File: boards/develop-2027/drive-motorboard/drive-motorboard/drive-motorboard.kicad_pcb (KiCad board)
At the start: 2 copper layers, 0 parts

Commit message: WIP layout draft
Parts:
- added C1: 100u 35V, Capacitor_SMD:C_Elec_6.3x5.8, B.Cu at (59.0, 66.0)
- added C10: 100n 10V, Capacitor_SMD:C_0402_1005Metric, F.Cu at (88.5, 85.2)
- added C11: 1n, Capacitor_SMD:C_0402_1005Metric, B.Cu at (77.2, 91.2)
- added C12: 1u 63V, Capacitor_SMD:C_0603_1608Metric, B.Cu at (73.5, 78.5)
- added C13: 1u 63V, Capacitor_SMD:C_0603_1608Metric, B.Cu at (70.5, 78.5)
- added C14: 1u 63V, Capacitor_SMD:C_0603_1608Metric, B.Cu at (67.5, 78.5)
- added C15: 1u 63V, Capacitor_SMD:C_0603_1608Metric, B.Cu at (64.5, 78.5)
- added C16: 1u 63V, Capacitor_SMD:C_0603_1608Metric, B.Cu at (61.5, 78.5)
- added C17: 1u 63V, Capacitor_SMD:C_0603_1608Metric, B.Cu at (58.5, 78.5)
- added C18: 100n 10V, Capacitor_SMD:C_0402_1005Metric, B.Cu at (83.2, 91.1)
- added C19: 100n 10V, Capacitor_SMD:C_0402_1005Metric, F.Cu at (70.6, 75.0)
- added C2: 1u 10V, Capacitor_SMD:C_0603_1608Metric, B.Cu at (91.0, 83.2)
- added C20: 1u 63V, Capacitor_SMD:C_0603_1608Metric, F.Cu at (145.8, 52.8)
- added C21: 10u 25V, Capacitor_SMD:C_0603_1608Metric, F.Cu at (145.8, 55.3)
- added C22: 10u 25V, Capacitor_SMD:C_0603_1608Metric, F.Cu at (145.8, 57.8)
- added C23: 100n 10V, Capacitor_SMD:C_0402_1005Metric, B.Cu at (53.5, 91.2)
- added C3: 1u 63V, Capacitor_SMD:C_0603_1608Metric, F.Cu at (79.6, 82.2)
- added C4: 1u 63V, Capacitor_SMD:C_0603_1608Metric, F.Cu at (79.6, 84.2)
- added C5: 1u 63V, Capacitor_SMD:C_0603_1608Metric, F.Cu at (79.6, 86.2)
- added C6: 100u 35V, Capacitor_SMD:C_Elec_6.3x5.8, B.Cu at (59.0, 73.8)
- added C7: 100n 10V, Capacitor_SMD:C_0402_1005Metric, B.Cu at (89.8, 83.8)
- added C8: 1u 63V, Capacitor_SMD:C_0603_1608Metric, B.Cu at (90.0, 86.2)
- added C9: 10u 25V, Capacitor_SMD:C_0603_1608Metric, F.Cu at (89.8, 85.5)
- added D1: FAULT, LED_SMD:LED_0603_1608Metric, F.Cu at (113.3, 74.7)
- added D10: PUSB3FR4Z, Package_DFN_QFN:Diodes_UDFN-10_1x2.5mm_P0.5mm, F.Cu at (124.5, 89.7)
- added D11: SMAJ22A, Diode_SMD:D_SMA, F.Cu at (147.8, 61.3)
- added D12: VBATT PWR, LED_SMD:LED_0603_1608Metric, F.Cu at (149.8, 57.4)
- added D2: 1N4148WL2-TP, Diode_SMD:D_SOD-882, B.Cu at (78.4, 81.5)
- added D3: 1N4148WL2-TP, Diode_SMD:D_SOD-882, B.Cu at (78.4, 79.5)
- added D4: 1N4148WL2-TP, Diode_SMD:D_SOD-882, B.Cu at (78.4, 85.5)
- added D5: 1N4148WL2-TP, Diode_SMD:D_SOD-882, B.Cu at (78.4, 83.5)
- added D6: 1N4148WL2-TP, Diode_SMD:D_SOD-882, B.Cu at (78.4, 89.5)
- added D7: 1N4148WL2-TP, Diode_SMD:D_SOD-882, B.Cu at (78.4, 87.5)
- added D8: PUSB3FR4Z, Package_DFN_QFN:Diodes_UDFN-10_1x2.5mm_P0.5mm, F.Cu at (83.0, 93.0)
- added D9: PUSB3FR4Z, Package_DFN_QFN:Diodes_UDFN-10_1x2.5mm_P0.5mm, F.Cu at (21.2, 69.2)
- added F1: 10A 60V, RJ-Passives:Fuse_2410_6125Metric, F.Cu at (148.1, 65.9)
- added H1: Motor Mount, MountingHole:MountingHole_3.2mm_M3_Pad, F.Cu at (96.0, 54.0)
- added H2: Motor Mount, MountingHole:MountingHole_3.2mm_M3_Pad, F.Cu at (96.0, 96.0)
- added H3: Motor Mount, MountingHole:MountingHole_3.2mm_M3_Pad, F.Cu at (54.0, 96.0)
- added H4: Motor Mount, MountingHole:MountingHole_3.2mm_M3_Pad, F.Cu at (54.0, 54.0)
- added J1: MOTOR HALL, Connector_JST:JST_ACH_BM05B-ACHSS-A-GAN-ETF_1x05-1MP_P1.20mm_Vertical, F.Cu at (83.0, 97.0)
- added J2: MOTOR UVW, Connector_JST:JST_ACH_BM03B-ACHSS-GAN-ETF_1x03-1MP_P1.20mm_Vertical, F.Cu at (66.0, 97.0)
- added J3: PROG SPI, Connector_JST:JST_GH_SM06B-GHS-TB_1x06-1MP_P1.25mm_Horizontal, F.Cu at (21.2, 64.2)
- added J4: COMM SPI, Connector_JST:JST_GH_SM06B-GHS-TB_1x06-1MP_P1.25mm_Horizontal, F.Cu at (85.0, 55.0)
- added J5: Conn_ST_STDC14, Connector:Tag-Connect_TC2070-IDC-FP_2x07_P1.27mm_Vertical, B.Cu at (92.0, 70.5)
- added J6: PWR_IN, Connector_JST:JST_VH_B2PS-VH_1x02_P3.96mm_Horizontal, F.Cu at (136.8, 53.9)
- added L1: 10u 540mA, Inductor_SMD:L_1210_3225Metric, F.Cu at (146.6, 70.2)
- added Q1: STL90N10F7, Package_DFN_QFN:PQFN-8-EP_6x5mm_P1.27mm_Generic, B.Cu at (72.0, 83.0)
- added Q2: STL90N10F7, Package_DFN_QFN:PQFN-8-EP_6x5mm_P1.27mm_Generic, B.Cu at (72.0, 90.5)
- added Q3: STL90N10F7, Package_DFN_QFN:PQFN-8-EP_6x5mm_P1.27mm_Generic, B.Cu at (66.0, 83.0)
- added Q4: STL90N10F7, Package_DFN_QFN:PQFN-8-EP_6x5mm_P1.27mm_Generic, B.Cu at (66.0, 90.5)
- added Q5: STL90N10F7, Package_DFN_QFN:PQFN-8-EP_6x5mm_P1.27mm_Generic, B.Cu at (60.0, 83.0)
- added Q6: STL90N10F7, Package_DFN_QFN:PQFN-8-EP_6x5mm_P1.27mm_Generic, B.Cu at (60.0, 90.5)
- added R1: 15m ±1% 3W, RJ-Passives:R_Shunt_Analog_2512_6332_HighAccuracy, B.Cu at (78.0, 97.0)
- added R10: 0R, Resistor_SMD:R_0402_1005Metric, B.Cu at (76.8, 79.0)
- added R11: 68R, Resistor_SMD:R_0402_1005Metric, B.Cu at (76.8, 85.0)
- added R12: 68R, Resistor_SMD:R_0402_1005Metric, B.Cu at (76.8, 84.0)
- added R13: 0R, Resistor_SMD:R_0402_1005Metric, B.Cu at (76.8, 86.0)
- added R14: 0R, Resistor_SMD:R_0402_1005Metric, B.Cu at (76.8, 83.0)
- added R15: 68R, Resistor_SMD:R_0402_1005Metric, B.Cu at (76.8, 89.0)
- added R16: 68R, Resistor_SMD:R_0402_1005Metric, B.Cu at (76.8, 88.0)
- added R17: 0R, Resistor_SMD:R_0402_1005Metric, B.Cu at (76.8, 90.0)
- added R18: 0R, Resistor_SMD:R_0402_1005Metric, B.Cu at (76.8, 87.0)
- added R19: 1.13k ±0.1%, Resistor_SMD:R_0402_1005Metric, B.Cu at (77.8, 93.8)
- added R2: 10k, Resistor_SMD:R_0402_1005Metric, F.Cu at (126.6, 52.5)
- added R20: 16.5k ±0.1%, Resistor_SMD:R_0402_1005Metric, F.Cu at (77.2, 92.2)
- added R21: 16.5k ±0.1%, Resistor_SMD:R_0402_1005Metric, F.Cu at (77.2, 91.2)
- added R22: 1.13k ±0.1%, Resistor_SMD:R_0402_1005Metric, B.Cu at (79.2, 93.8)
- added R23: 8.25k ±0.5%, Resistor_SMD:R_0201_0603Metric, B.Cu at (83.0, 89.5)
- added R24: 300R ±1%, Resistor_SMD:R_0201_0603Metric, B.Cu at (83.5, 90.2)
- added R25: 10k, Resistor_SMD:R_0402_1005Metric, B.Cu at (88.5, 79.8)
- added R26: 10k, Resistor_SMD:R_0402_1005Metric, B.Cu at (87.5, 79.8)
- added R27: 10k, Resistor_SMD:R_0402_1005Metric, B.Cu at (85.2, 79.8)
- added R28: 10k, Resistor_SMD:R_0402_1005Metric, B.Cu at (21.8, 64.0)
- added R29: 10k, Resistor_SMD:R_0402_1005Metric, B.Cu at (19.4, 64.0)
- added R3: 10k, Resistor_SMD:R_0402_1005Metric, F.Cu at (89.2, 83.2)
- added R30: 10k, Resistor_SMD:R_0402_1005Metric, B.Cu at (23.0, 64.0)
- added R31: 4.7k, Resistor_SMD:R_0402_1005Metric, F.Cu at (53.8, 87.2)
- added R32: 4.7k, Resistor_SMD:R_0402_1005Metric, F.Cu at (54.8, 87.2)
- added R33: 10k, Resistor_SMD:R_0402_1005Metric, F.Cu at (126.7, 79.0)
- added R34: 100, Resistor_SMD:R_0402_1005Metric, F.Cu at (92.0, 68.4)
- added R35: 100k, Resistor_SMD:R_0402_1005Metric, F.Cu at (150.8, 69.1)
- added R36: 10k, Resistor_SMD:R_0402_1005Metric, F.Cu at (150.8, 71.1)
- added R4: 1.13k ±0.1%, Resistor_SMD:R_0402_1005Metric, B.Cu at (76.8, 93.8)
- added R5: 33k ±0.1%, Resistor_SMD:R_0402_1005Metric, B.Cu at (77.2, 92.2)
- added R6: 10k, Resistor_SMD:R_0402_1005Metric, F.Cu at (126.6, 60.5)
- added R7: 68R, Resistor_SMD:R_0402_1005Metric, B.Cu at (76.8, 81.0)
- added R8: 68R, Resistor_SMD:R_0402_1005Metric, B.Cu at (76.8, 80.0)
- added R9: 0R, Resistor_SMD:R_0402_1005Metric, B.Cu at (76.8, 82.0)
- added SW1: RESET, Button_Switch_SMD:SW_Push_1P1T_NO_CK_KMR2, F.Cu at (128.5, 63.8)
- added U1: STSPIN32G0B2, Package_DFN_QFN:VQFN-48-1EP_7x7mm_P0.5mm_EP2.6x2.6mm, B.Cu at (85.0, 85.0)
- added U2: AS5047P, Package_SO:TSSOP-14_4.4x5mm_P0.65mm, F.Cu at (75.0, 75.0)
- added U3: LM75ADP, Package_SO:TSSOP-8_3x3mm_P0.65mm, B.Cu at (55.0, 87.8)
- added U4: TPS62177DQC, Package_SON:WSON-10-1EP_2x3mm_P0.5mm_EP0.84x2.4mm_ThermalVias, F.Cu at (149.9, 53.8)
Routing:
- net /Motor Controller/I2C.SDA: track 0.00 -> 46.8 mm, vias 0 -> 2
- net /Motor Controller/I2C.SCL: track 0.00 -> 43.8 mm, vias 0 -> 2
- net /External Connections/USART.RX: track 0.00 -> 30.0 mm, vias 0 -> 2
- net /External Connections/USART.TX: track 0.00 -> 27.2 mm, vias 0 -> 2
- net /External Connections/~{RST}: track 0.00 -> 23.6 mm, vias 0 -> 2
- net /Magnetic Encoder/ENC.A: track 0.00 -> 20.3 mm, vias 0 -> 2
- net /Motor Connections/HALL.C: track 0.00 -> 19.7 mm, vias 0 -> 2
- net /Magnetic Encoder/ENC.B: track 0.00 -> 19.4 mm, vias 0 -> 2
- net /Motor Connections/HALL.B: track 0.00 -> 19.0 mm, vias 0 -> 2
- net /Motor Connections/HALL.A: track 0.00 -> 17.6 mm, vias 0 -> 2
- net /External Connections/SWD.IO: track 0.00 -> 17.2 mm, vias 0 -> 2
- net /External Connections/SWD.CLK: track 0.00 -> 15.5 mm
- net /Motor Controller/Current Sensing/OPxP: track 0.00 -> 8.84 mm, vias 0 -> 1
- net +3.3V: track 0.00 -> 8.34 mm, vias 0 -> 10
- net Net-(U1Over-Current-OCCOMP): track 0.00 -> 8.08 mm
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- added copper zone on In1.Cu, net GND
- added copper zone on In3.Cu, net GND
- added copper zone on In4.Cu, net GND
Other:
- board outline added: 50 x 50 mm
- copper layers 2 -> 6
- board text added: "FRONT IS TOWARDS MOTOR BACK SHELL BACK IS AWAY FROM MOTOR BACK SHELL"
- board text added: "Maximum Height in Circle 5 mm (Front)"
- board text added: "Wires In"

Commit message: add new mechanical specification
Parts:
- J4, J6: moved to B.Cu
- moved J4 162.1 mm to (247.0, 49.0), turned to 90 degrees
- moved H1 135.1 mm to (231.0, 58.0)
- moved H2 135.1 mm to (231.0, 100.0)
- moved H3 135.1 mm to (189.0, 100.0)
- moved H4 135.1 mm to (189.0, 58.0)
- moved J2 124.1 mm to (180.0, 48.0)
- moved J1 121.3 mm to (194.0, 48.0)
- moved J6 72.1 mm to (205.8, 33.0), turned to 90 degrees
- moved C19 5.50 mm to (70.6, 69.5)
- moved U2 5.50 mm to (75.0, 69.5)
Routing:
- net /Motor Controller/I2C.SDA: track 46.8 -> 0.00 mm, vias 2 -> 0
- net /Motor Controller/I2C.SCL: track 43.8 -> 0.00 mm, vias 2 -> 0
- net /External Connections/USART.RX: track 30.0 -> 0.00 mm, vias 2 -> 0
- net /External Connections/USART.TX: track 27.2 -> 0.00 mm, vias 2 -> 0
- net /External Connections/~{RST}: track 23.6 -> 0.00 mm, vias 2 -> 0
- net /Magnetic Encoder/ENC.A: track 20.3 -> 0.00 mm, vias 2 -> 0
- net /Motor Connections/HALL.C: track 19.7 -> 0.00 mm, vias 2 -> 0
- net /Magnetic Encoder/ENC.B: track 19.4 -> 0.00 mm, vias 2 -> 0
- net /Motor Connections/HALL.B: track 19.0 -> 0.00 mm, vias 2 -> 0
- net /Motor Connections/HALL.A: track 17.6 -> 0.00 mm, vias 2 -> 0
- net /External Connections/SWD.IO: track 17.2 -> 0.00 mm, vias 2 -> 0
- net /External Connections/SWD.CLK: track 15.5 -> 0.00 mm
- net /Motor Controller/Current Sensing/OPxP: track 8.84 -> 0.00 mm, vias 1 -> 0
- net +3.3V: track 8.34 -> 0.00 mm, vias 10 -> 0
- net Net-(U1Over-Current-OCCOMP): track 8.08 -> 0.00 mm
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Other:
- board size 50 x 50 mm -> 185 x 54 mm
- board text added: "Back Side: Component Height <5mm under this line"
- board text added: "DOWN"
- board text added: "Use Vertical connectors for power/data"

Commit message: fix mess caused by multiple variants
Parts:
- added J7: Conn_ST_STDC14, Connector_PinHeader_1.27mm:PinHeader_2x07_P1.27mm_Vertical_SMD, F.Cu at (128.8, 160.5)
- added R37: 100, Resistor_SMD:R_0402_1005Metric, F.Cu at (126.5, 150.5)
- C1, C11, C12, C13, C14, C15, C16, C17, C2, C23, C6, C7, C8, D2, D3, D4, D5, D6, D7, J5, Q1, Q2, Q3, Q4, Q5, Q6, R1, R10, R11, R12, R13, R14, R15, R16, R17, R18, R19, R22, R23, R24, R25, R26, R27, R28, R29, R30, R4, R5, R7, R8, R9, U1, U3: moved to F.Cu
- C18: value 100n 10V -> 100n; moved to F.Cu
- C19: value 100n 10V -> 100n
- F1: value 10A 60V -> 10A 63V; footprint RJ-Passives:Fuse_2410_6125Metric -> Fuse:Fuse_1206_3216Metric_Pad1.42x1.75mm_HandSolder
- J4: footprint Connector_JST:JST_GH_SM06B-GHS-TB_1x06-1MP_P1.25mm_Horizontal -> Connector_JST:JST_GH_BM06B-GHS-TBT_1x06-1MP_P1.25mm_Vertical; moved to F.Cu
- J6: footprint Connector_JST:JST_VH_B2PS-VH_1x02_P3.96mm_Horizontal -> Connector_JST:JST_VH_B2P-VH-B_1x02_P3.96mm_Vertical
- moved J4 164.3 mm to (86.2, 82.8), turned to 0 degrees
- moved J6 153.5 mm to (55.5, 64.8)
- moved R29 149.4 mm to (113.9, 179.8), turned to 0 degrees
- moved R30 148.7 mm to (113.9, 181.8), turned to 0 degrees
- moved R28 146.4 mm to (113.9, 177.8), turned to 0 degrees
- moved D9 145.5 mm to (116.8, 178.9), turned to 0 degrees
- moved C20 137.8 mm to (95.6, 181.2)
- moved C21 137.8 mm to (95.6, 183.7)
- moved C22 137.8 mm to (95.6, 186.2)
- moved C15 135.5 mm to (130.6, 196.8), turned to 0 degrees
- moved H1 135.1 mm to (96.0, 54.0)
- moved H2 135.1 mm to (96.0, 96.0)
- moved H3 135.1 mm to (54.0, 96.0)
- moved H4 135.1 mm to (54.0, 54.0)
- moved F1 134.2 mm to (88.5, 186.1)
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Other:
- board size 185 x 54 mm -> 50 x 50 mm
- board text added: "Front: Max part height 5mm in circle Back: Max part height 5mm below dotted line"
- board text added: "Front: Towards Motor Back: Away from Motor"
- board text removed: "Back Side: Component Height <5mm under this line"
- board text removed: "FRONT IS TOWARDS MOTOR BACK SHELL BACK IS AWAY FROM MOTOR BACK SHELL"
- board text removed: "Maximum Height in Circle 5 mm (Front)"
- board text removed: "Use Vertical connectors for power/data"
- board text removed: "Wires In"

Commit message: finalize mechanical outline
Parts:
- added REF**: JST_VH_B2PS-VH_1x02_P3.96mm_Horizontal, Connector_JST:JST_VH_B2PS-VH_1x02_P3.96mm_Horizontal, F.Cu at (89.0, 96.8)
- J3: footprint Connector_JST:JST_GH_SM06B-GHS-TB_1x06-1MP_P1.25mm_Horizontal -> Connector_JST:JST_GH_BM06B-GHS-TBT_1x06-1MP_P1.25mm_Vertical
- J4, R28, R29, R30: moved to B.Cu
- moved C19 109.9 mm to (70.5, 82.2), turned to -90 degrees
- moved U2 103.2 mm to (75.0, 82.5), turned to 180 degrees
- moved D9 97.4 mm to (75.0, 91.0), turned to 90 degrees
- moved R30 92.9 mm to (77.0, 96.5), turned to 90 degrees
- moved R29 92.8 mm to (73.0, 96.5), turned to -90 degrees
- moved J6 91.2 mm to (112.5, 136.0)
- moved R28 90.1 mm to (75.0, 96.5), turned to -90 degrees
- moved J5 87.8 mm to (65.0, 155.0)
- moved J4 25.0 mm to (65.0, 96.0)
- moved J1 18.1 mm to (62.5, 53.0), turned to 180 degrees
- moved J2 16.3 mm to (87.5, 53.0), turned to 180 degrees
- moved J3 5.01 mm to (75.0, 96.0), turned to 180 degrees
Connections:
- D9 pad 1: /Magnetic Encoder/PROGSPI.CSN -> /Magnetic Encoder/PROGSPI.MOSI
- D9 pad 2: /Magnetic Encoder/PROGSPI.CLK -> /Magnetic Encoder/PROGSPI.MISO
- D9 pad 4: /Magnetic Encoder/PROGSPI.MISO -> /Magnetic Encoder/PROGSPI.CLK
- D9 pad 5: /Magnetic Encoder/PROGSPI.MOSI -> /Magnetic Encoder/PROGSPI.CSN
- J3 pad 2: /Magnetic Encoder/PROGSPI.MOSI -> /Magnetic Encoder/PROGSPI.CSN
- J3 pad 3: /Magnetic Encoder/PROGSPI.MISO -> /Magnetic Encoder/PROGSPI.CLK
- J3 pad 4: /Magnetic Encoder/PROGSPI.CLK -> /Magnetic Encoder/PROGSPI.MISO
- J3 pad 5: /Magnetic Encoder/PROGSPI.CSN -> /Magnetic Encoder/PROGSPI.MOSI
- R28 pad 1: /Magnetic Encoder/PROGSPI.MISO -> /Magnetic Encoder/PROGSPI.CLK
- R29 pad 1: /Magnetic Encoder/PROGSPI.CSN -> /Magnetic Encoder/PROGSPI.MOSI
- R30 pad 2: /Magnetic Encoder/PROGSPI.MOSI -> /Magnetic Encoder/PROGSPI.CSN
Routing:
- net /Magnetic Encoder/PROGSPI.MOSI: track 0.00 -> 17.2 mm, vias 0 -> 1
- net /Magnetic Encoder/PROGSPI.CLK: track 0.00 -> 14.3 mm, vias 0 -> 1
- net /Magnetic Encoder/PROGSPI.MISO: track 0.00 -> 14.0 mm
- net /Magnetic Encoder/PROGSPI.CSN: track 0.00 -> 13.5 mm, vias 0 -> 1
- net GND: track 0.00 -> 2.00 mm, vias 0 -> 2
- added copper zone on In2.Cu, net +3.3V
- added copper zone on B.Cu, net GND
- added copper zone on F.Cu, net GND

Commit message: proposed connector placement
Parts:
- removed C1, C6: 100u 35V, Capacitor_SMD:C_Elec_6.3x5.8
- removed C10, C23, C7: 100n 10V, Capacitor_SMD:C_0402_1005Metric
- removed C11: 1n, Capacitor_SMD:C_0402_1005Metric
- removed C12, C13, C14, C15, C16, C17, C20, C3, C4, C5, C8: 1u 63V, Capacitor_SMD:C_0603_1608Metric
- removed C18: 100n, Capacitor_SMD:C_0402_1005Metric
- removed C2: 1u 10V, Capacitor_SMD:C_0603_1608Metric
- removed C21, C22, C9: 10u 25V, Capacitor_SMD:C_0603_1608Metric
- removed D1: FAULT, LED_SMD:LED_0603_1608Metric
- removed D10, D8: PUSB3FR4Z, Package_DFN_QFN:Diodes_UDFN-10_1x2.5mm_P0.5mm
- removed D11: SMAJ22A, Diode_SMD:D_SMA
- removed D12: VBATT PWR, LED_SMD:LED_0603_1608Metric
- removed D2, D3, D4, D5, D6, D7: 1N4148WL2-TP, Diode_SMD:D_SOD-882
- removed F1: 10A 63V, Fuse:Fuse_1206_3216Metric_Pad1.42x1.75mm_HandSolder
- removed J5: Conn_ST_STDC14, Connector:Tag-Connect_TC2070-IDC-FP_2x07_P1.27mm_Vertical
- removed J7: Conn_ST_STDC14, Connector_PinHeader_1.27mm:PinHeader_2x07_P1.27mm_Vertical_SMD
- removed L1: 10u 540mA, Inductor_SMD:L_1210_3225Metric
- removed Q1, Q2, Q3, Q4, Q5, Q6: STL90N10F7, Package_DFN_QFN:PQFN-8-EP_6x5mm_P1.27mm_Generic
- removed R1: 15m ±1% 3W, RJ-Passives:R_Shunt_Analog_2512_6332_HighAccuracy
- removed R10, R13, R14, R17, R18, R9: 0R, Resistor_SMD:R_0402_1005Metric
- removed R11, R12, R15, R16, R7, R8: 68R, Resistor_SMD:R_0402_1005Metric
- removed R19, R22, R4: 1.13k ±0.1%, Resistor_SMD:R_0402_1005Metric
- removed R2, R25, R26, R27, R3, R33, R36, R6: 10k, Resistor_SMD:R_0402_1005Metric
- removed R20, R21: 16.5k ±0.1%, Resistor_SMD:R_0402_1005Metric
- removed R23: 8.25k ±0.5%, Resistor_SMD:R_0201_0603Metric
- removed R24: 300R ±1%, Resistor_SMD:R_0201_0603Metric
- removed R31, R32: 4.7k, Resistor_SMD:R_0402_1005Metric
- removed R34, R37: 100, Resistor_SMD:R_0402_1005Metric
- removed R35: 100k, Resistor_SMD:R_0402_1005Metric
- removed R5: 33k ±0.1%, Resistor_SMD:R_0402_1005Metric
- removed REF**: JST_VH_B2PS-VH_1x02_P3.96mm_Horizontal, Connector_JST:JST_VH_B2PS-VH_1x02_P3.96mm_Horizontal
- removed SW1: RESET, Button_Switch_SMD:SW_Push_1P1T_NO_CK_KMR2
- removed U1: STSPIN32G0B2, Package_DFN_QFN:VQFN-48-1EP_7x7mm_P0.5mm_EP2.6x2.6mm
- removed U3: LM75ADP, Package_SO:TSSOP-8_3x3mm_P0.65mm
- removed U4: TPS62177DQC, Package_SON:WSON-10-1EP_2x3mm_P0.5mm_EP0.84x2.4mm_ThermalVias
- J3, J4: footprint Connector_JST:JST_GH_BM06B-GHS-TBT_1x06-1MP_P1.25mm_Vertical -> Connector_JST:JST_GH_SM06B-GHS-TB_1x06-1MP_P1.25mm_Horizontal
- J6: footprint Connector_JST:JST_VH_B2P-VH-B_1x02_P3.96mm_Vertical -> Connector_JST:JST_PH_S4B-PH-SM4-TB_1x04-1MP_P2.00mm_Horizontal
- moved J6 50.2 mm to (85.0, 94.0), turned to 0 degrees
- moved J2 3.50 mm to (84.0, 53.0)
- moved R29 3.00 mm to (76.0, 96.5)
- moved R30 3.00 mm to (74.0, 96.5)
- moved J1 2.00 mm to (64.5, 53.0)
- moved J4 1.00 mm to (65.0, 95.0)
- turned D9 to -90 degrees
- turned J3 to 0 degrees
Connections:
- D9 pad 1: /Magnetic Encoder/PROGSPI.MOSI -> /Magnetic Encoder/PROGSPI.CSN
- D9 pad 2: /Magnetic Encoder/PROGSPI.MISO -> /Magnetic Encoder/PROGSPI.CLK
- D9 pad 4: /Magnetic Encoder/PROGSPI.CLK -> /Magnetic Encoder/PROGSPI.MISO
- D9 pad 5: /Magnetic Encoder/PROGSPI.CSN -> /Magnetic Encoder/PROGSPI.MOSI
- J3 pad 2: /Magnetic Encoder/PROGSPI.CSN -> /Magnetic Encoder/PROGSPI.MOSI
- J3 pad 3: /Magnetic Encoder/PROGSPI.CLK -> /Magnetic Encoder/PROGSPI.MISO
- J3 pad 4: /Magnetic Encoder/PROGSPI.MISO -> /Magnetic Encoder/PROGSPI.CLK
- J3 pad 5: /Magnetic Encoder/PROGSPI.MOSI -> /Magnetic Encoder/PROGSPI.CSN
- J6 pad 2: Net-(J6-Pin_2) -> GND
- R28 pad 1: /Magnetic Encoder/PROGSPI.CLK -> /Magnetic Encoder/PROGSPI.MISO
- R29 pad 1: /Magnetic Encoder/PROGSPI.MOSI -> /Magnetic Encoder/PROGSPI.CSN
- R30 pad 2: /Magnetic Encoder/PROGSPI.CSN -> /Magnetic Encoder/PROGSPI.MOSI
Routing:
- net /Magnetic Encoder/PROGSPI.MOSI: track 17.2 -> 4.28 mm, vias 1 -> 0
- net /Magnetic Encoder/PROGSPI.CLK: track 14.3 -> 2.76 mm, vias 1 -> 0
- net /Magnetic Encoder/PROGSPI.CSN: track 13.5 -> 2.09 mm, vias 1 -> 0
- net /Magnetic Encoder/PROGSPI.MISO: track 14.0 -> 3.61 mm
- net GND: track 2.00 -> 0.00 mm, vias 2 -> 0

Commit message: add proper stackup
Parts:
- removed J3: PROG SPI, Connector_JST:JST_GH_SM06B-GHS-TB_1x06-1MP_P1.25mm_Horizontal

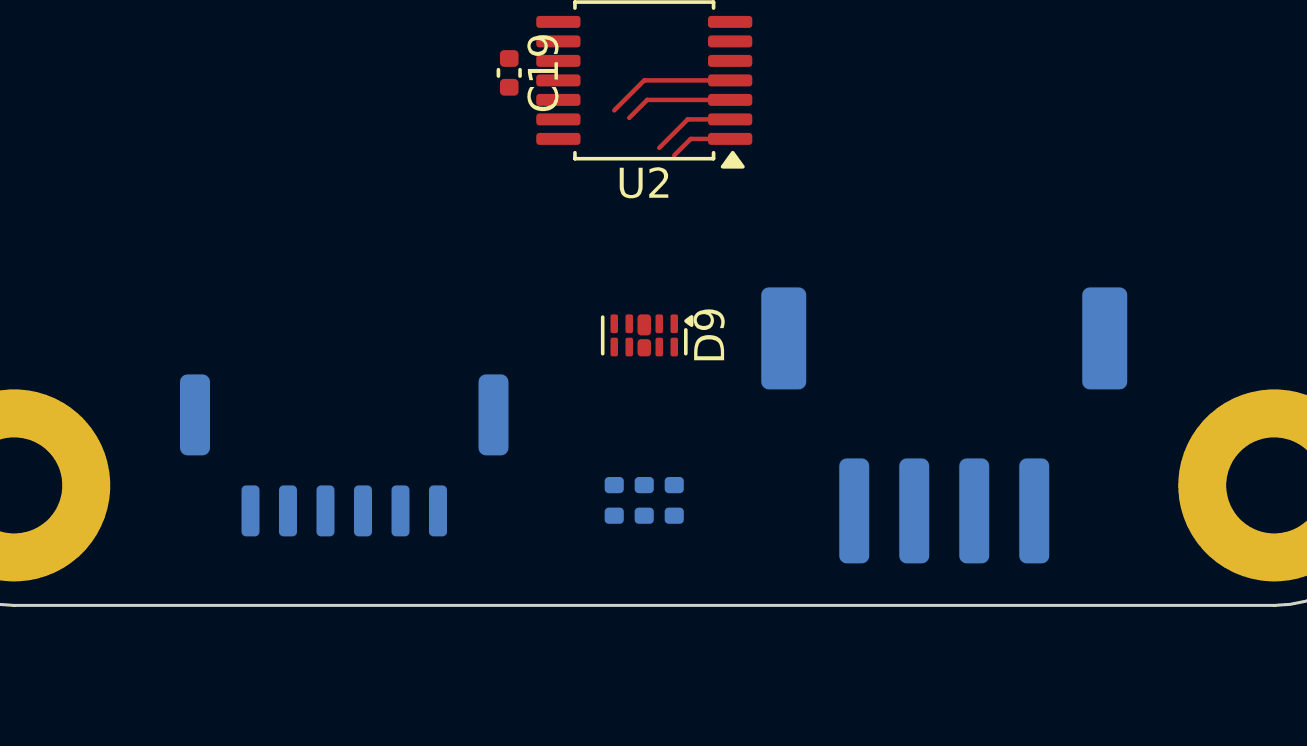
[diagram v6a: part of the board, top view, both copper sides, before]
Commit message: Add mechanical constraints
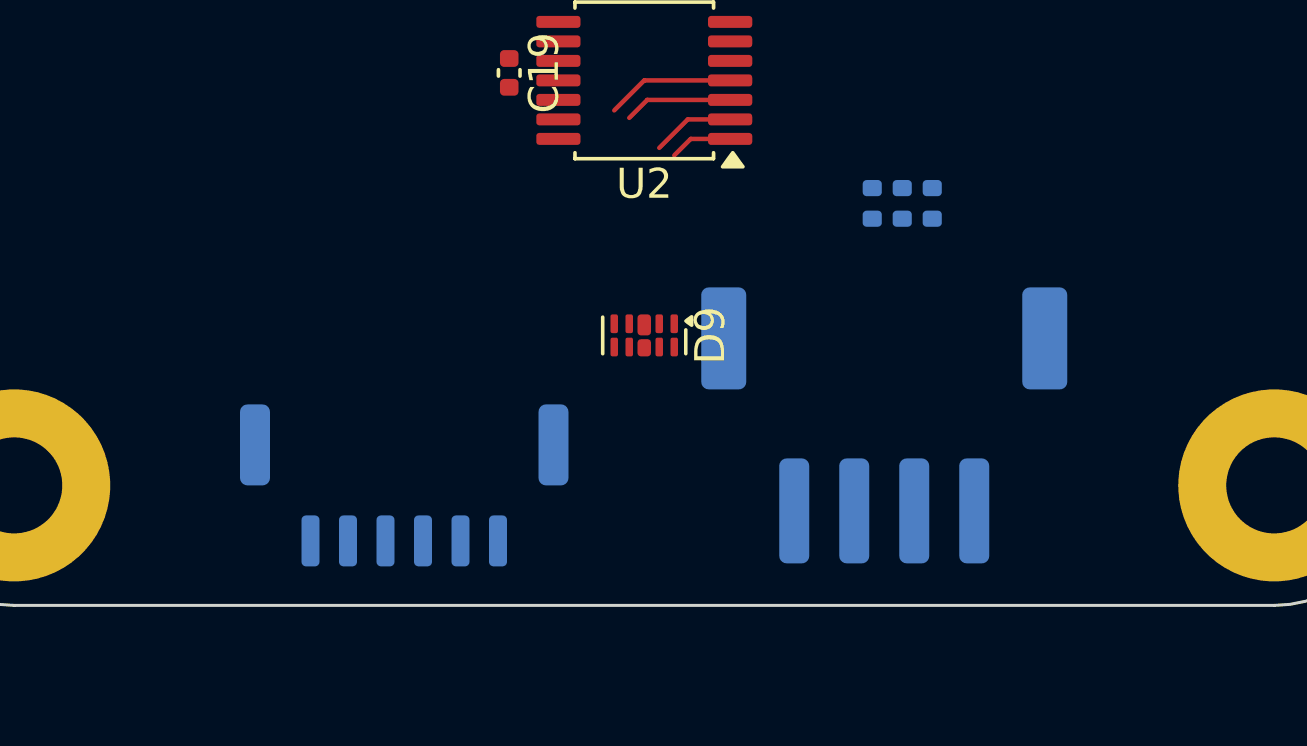
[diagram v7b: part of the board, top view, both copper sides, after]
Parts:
- moved R28 13.1 mm to (83.6, 86.6)
- moved R29 13.1 mm to (84.6, 86.6)
- moved R30 13.1 mm to (82.6, 86.6)
- moved J4 2.24 mm to (67.0, 96.0)
- moved J6 2.00 mm to (83.0, 94.0)
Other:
- board text added: "30°"
- board text added: "Back Side below dashed line: Parts must fit within below area"
- board text added: "Front: Max part height 5mm in circle Back: Max part height 30mm above dotted line Consult diagram for below dotted line"
- board text added: "Side View"
- board text added: "To Scale"
- board text removed: "Front: Max part height 5mm in circle Back: Max part height 5mm below dotted line"
